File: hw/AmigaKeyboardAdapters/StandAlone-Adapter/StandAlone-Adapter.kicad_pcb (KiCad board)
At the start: 2 copper layers, 78.7 x 58.4 mm, 56 parts, among them J1 RJ12, J2 Conn_02x03_Odd_Even, P1 CONN_01X02, Q1 BSS138, Q2 BSS138, Q3 BSS138, U1 AZ1117-3.3, U3 STM32F401RCTx

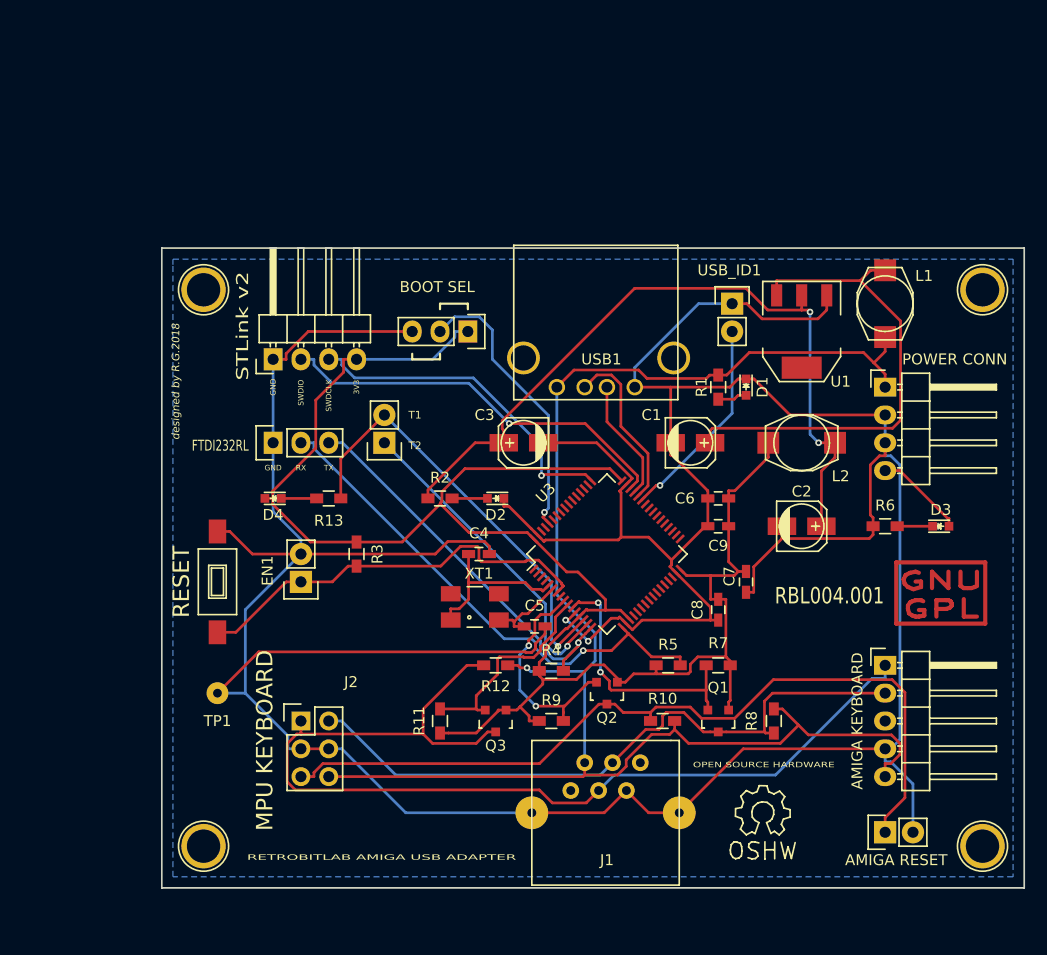
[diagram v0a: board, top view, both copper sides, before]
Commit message: Modified for USB Host A and RJ10 Connectors
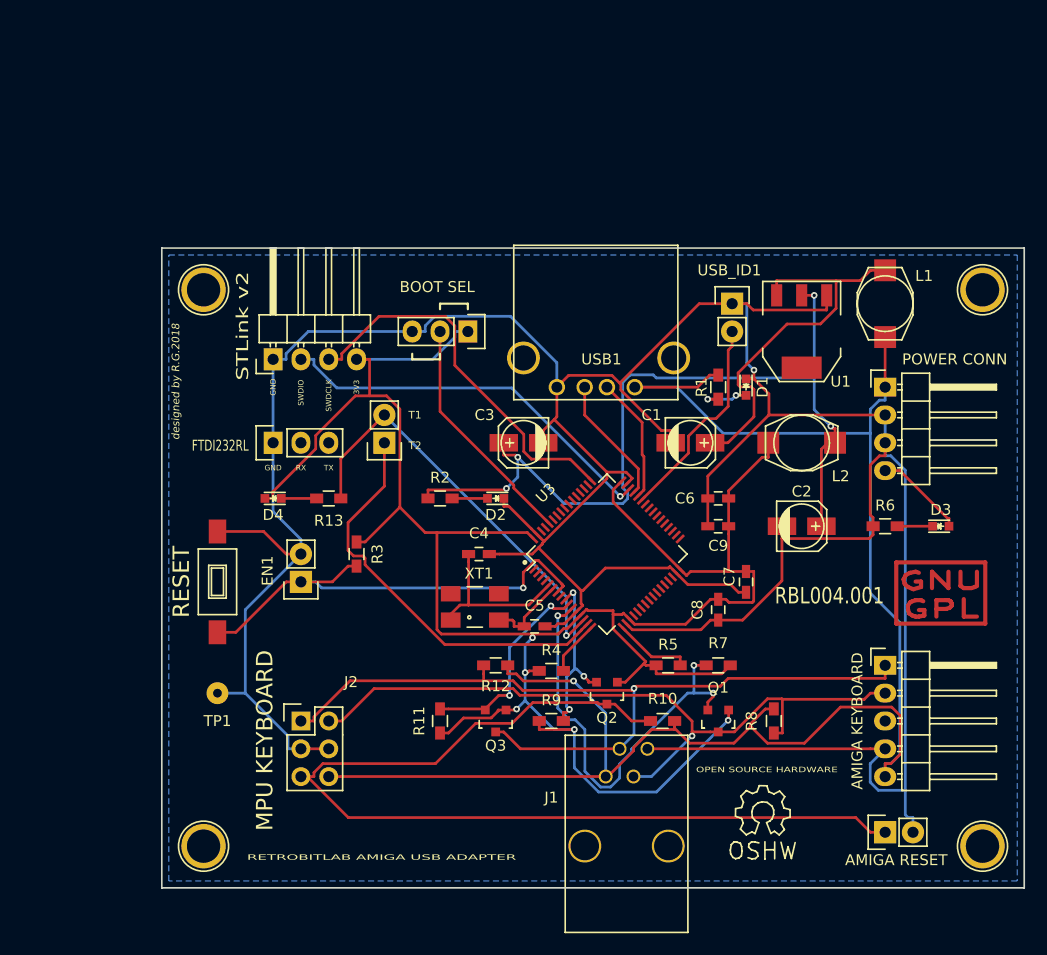
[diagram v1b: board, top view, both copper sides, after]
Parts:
- J1: value RJ12 -> RJ10; footprint Connect:RJ12_E -> RetroBitLab:RJ10-RECEPTACLE-Assmann-ASS-2004-3-4-LP-N-R
- moved J1 12.0 mm to (158.8, 130.8)
- renumbered G*** to AMIGALOGO, REF** to GNUGPL, G*** to WORKBENCHLOGO
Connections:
- DEBUG1 pad 2: UART_RX_TTL -> (no net)
- DEBUG1 pad 3: UART_TX_TTL -> (no net)
- J1 pad 1: (no net) -> VCC5V
- J1 pad 2: VCC5V -> KBD_CLOCK
- J1 pad 3: KBD_CLOCK -> KBD_DATA
- J1 pad 4: KBD_DATA -> GND
- J1 pad 5: GND -> (no net)
- R4 pad 2: UART_TX_TTL -> /USART3_TX
- R5 pad 2: UART_RX_TTL -> /USART3_RX
- U3 pad 16: UART_TX_TTL -> /USART3_TX
- U3 pad 17: UART_RX_TTL -> /USART3_RX
- USB1 pad 1: GND -> VCC5V
- USB1 pad 2: USB_P -> USB_N
- USB1 pad 3: USB_N -> USB_P
- USB1 pad 4: VCC5V -> GND
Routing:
- net UART_RX_TTL: track 47.2 -> 0.00 mm, vias 1 -> 0
- net GND: track 371.1 -> 332.7 mm, vias 2 -> 1
- net UART_TX_TTL: track 37.1 -> 0.00 mm, vias 1 -> 0
- net VCC3V3: track 167.8 -> 203.1 mm, vias 0 -> 5
- net KBD_CLOCK: track 95.6 -> 76.5 mm, vias 0 -> 1
- net KBD_3v3_DATA: track 23.9 -> 39.4 mm, vias 2 -> 3
- net KBD_RESET: track 75.3 -> 90.5 mm
- net VCC5V: track 144.9 -> 159.1 mm
- net Net-(C2-Pad1): track 68.8 -> 78.7 mm, vias 2 -> 4
- net +5V: track 44.8 -> 35.7 mm
- net TP2: track 30.1 -> 37.8 mm, vias 1 -> 0
- net /USART3_RX: track 0.00 -> 7.20 mm
- net KBD_DATA: track 60.5 -> 66.8 mm, vias 0 -> 1
- net Net-(EN1-Pad1): track 37.9 -> 43.1 mm, vias 0 -> 1
- net /USART3_TX: track 0.00 -> 5.06 mm
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
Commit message: The Debug UART Pins (RX & TX) were left unconnected
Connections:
- DEBUG1 pad 2: (no net) -> UART_RX_TTL
- DEBUG1 pad 3: (no net) -> UART_TX_TTL
- R4 pad 2: /USART3_TX -> UART_TX_TTL
- R5 pad 2: /USART3_RX -> UART_RX_TTL
- U3 pad 16: /USART3_TX -> UART_TX_TTL
- U3 pad 17: /USART3_RX -> UART_RX_TTL
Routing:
- net UART_RX_TTL: track 0.00 -> 150.0 mm, vias 0 -> 4
- net UART_TX_TTL: track 0.00 -> 78.3 mm, vias 0 -> 1
- net /USART3_RX: track 7.20 -> 0.00 mm
- net /USART3_TX: track 5.06 -> 0.00 mm
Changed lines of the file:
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@@
 (kicad_pcb (version 4) (host pcbnew 4.0.2+dfsg1-stable)
   (general
-    (links 108)
+    (links 110)
     (no_connects 0)
     (area 121.844999 86.284999 200.735001 144.855001)
     (thickness 1.6)
     (drawings 35)
-    (tracks 550)
+    (tracks 583)
     (zones 0)
     (modules 56)
@@
     (34 B.Paste user)
     (35 F.Paste user)
-    (36 B.SilkS user)
-    (37 F.SilkS user)
+    (36 B.SilkS user hide)
+    (37 F.SilkS user hide)
     (38 B.Mask user)
     (39 F.Mask user)
@@
   (net 26 USB_N)
   (net 27 USB_P)
-  (net 28 /USART3_TX)
-  (net 29 /USART3_RX)
+  (net 28 UART_RX_TTL)
+  (net 29 UART_TX_TTL)
   (net_class Default "This is the default net class."
     (clearance 0.2)
@@
     (uvia_drill 0.1)
     (add_net +5V)
-    (add_net /USART3_RX)
-    (add_net /USART3_TX)
     (add_net BOOT0)
     (add_net GND)
@@
     (add_net TP1)
     (add_net TP2)
+    (add_net UART_RX_TTL)
+    (add_net UART_TX_TTL)
     (add_net USB_ID)
     (add_net USB_N)
@@
     (pad 1 thru_hole rect (at 0 0 90) (size 2.032 1.7272) (drill 1.016) (layers *.Cu *.Mask F.SilkS)
       (net 3 GND))
-    (pad 2 thru_hole oval (at 0 2.54 90) (size 2.032 1.7272) (drill 1.016) (layers *.Cu *.Mask F.SilkS))
-    (pad 3 thru_hole oval (at 0 5.08 90) (size 2.032 1.7272) (drill 1.016) (layers *.Cu *.Mask F.SilkS))
+    (pad 2 thru_hole oval (at 0 2.54 90) (size 2.032 1.7272) (drill 1.016) (layers *.Cu *.Mask F.SilkS)
+      (net 28 UART_RX_TTL))
+    (pad 3 thru_hole oval (at 0 5.08 90) (size 2.032 1.7272) (drill 1.016) (layers *.Cu *.Mask F.SilkS)
+      (net 29 UART_TX_TTL))
     (model Pin_Headers.3dshapes/Pin_Header_Straight_1x03.wrl
       (at (xyz 0 -0.1 0))
@@
       (net 5 VCC3V3))
     (pad 2 smd rect (at 1.1 0) (size 1.2 0.9) (layers F.Cu F.Paste F.Mask)
-      (net 28 /USART3_TX))
+      (net 29 UART_TX_TTL))
     (model Resistors_SMD.3dshapes/R_0603_HandSoldering.wrl
       (at (xyz 0 0 0))
@@
       (net 5 VCC3V3))
     (pad 2 smd rect (at 1.1 0) (size 1.2 0.9) (layers F.Cu F.Paste F.Mask)
-      (net 29 /USART3_RX))
+      (net 28 UART_RX_TTL))
     (model Resistors_SMD.3dshapes/R_0603_HandSoldering.wrl
       (at (xyz 0 0 0))
@@
       (net 24 TP2))
     (pad 16 smd rect (at -5.7 3.75 45) (size 1 0.25) (layers F.Cu F.Paste F.Mask)
-      (net 28 /USART3_TX))
+      (net 29 UART_TX_TTL))
     (pad 17 smd rect (at -3.75 5.7 135) (size 1 0.25) (layers F.Cu F.Paste F.Mask)
-      (net 29 /USART3_RX))
+      (net 28 UART_RX_TTL))
     (pad 18 smd rect (at -3.25 5.7 135) (size 1 0.25) (layers F.Cu F.Paste F.Mask)
       (net 3 GND))
@@
   (segment (start 160.5271 101.6083) (end 165.4254 106.5066) (width 0.25) (layer F.Cu) (net 27))
   (segment (start 160.5271 99.0621) (end 160.5271 101.6083) (width 0.25) (layer F.Cu) (net 27))
-  (segment (start 158.58 123.5833) (end 158.58 124.968) (width 0.25) (layer F.Cu) (net 28))
-  (segment (start 161.1811 120.9822) (end 158.58 123.5833) (width 0.25) (layer F.Cu) (net 28))
-  (segment (start 166.6414 123.6847) (end 169.248 123.6847) (width 0.25) (layer F.Cu) (net 29))
-  (segment (start 163.9389 120.9822) (end 166.6414 123.6847) (width 0.25) (layer F.Cu) (net 29))
-  (segment (start 169.248 124.46) (end 169.248 123.6847) (width 0.25) (layer F.Cu) (net 29))
+  (segment (start 169.248 124.46) (end 169.248 122.8295) (width 0.25) (layer F.Cu) (net 28) (status 400000))
+  (segment (start 134.62 101.6) (end 134.62 104.14) (width 0.25) (layer F.Cu) (net 28) (status 800000))
+  (segment (start 134.5565 101.5365) (end 134.62 101.6) (width 0.25) (layer F.Cu) (net 28))
+  (segment (start 129.032 101.5365) (end 134.5565 101.5365) (width 0.25) (layer F.Cu) (net 28))
+  (via (at 129.032 101.5365) (size 0.6) (drill 0.4) (layers F.Cu B.Cu) (net 28))
+  (segment (start 129.032 89.2175) (end 129.032 101.5365) (width 0.25) (layer B.Cu) (net 28))
+  (segment (start 129.6035 88.646) (end 129.032 89.2175) (width 0.25) (layer B.Cu) (net 28))
+  (segment (start 183.3245 88.646) (end 129.6035 88.646) (width 0.25) (layer B.Cu) (net 28))
+  (segment (start 185.4835 90.805) (end 183.3245 88.646) (width 0.25) (layer B.Cu) (net 28))
+  (via (at 185.4835 90.805) (size 0.6) (drill 0.4) (layers F.Cu B.Cu) (net 28))
+  (segment (start 192.0875 90.805) (end 185.4835 90.805) (width 0.25) (layer F.Cu) (net 28))
+  (segment (start 197.104 95.8215) (end 192.0875 90.805) (width 0.25) (layer F.Cu) (net 28))
+  (segment (start 197.104 112.649) (end 197.104 95.8215) (width 0.25) (layer F.Cu) (net 28))
+  (segment (start 196.215 113.538) (end 197.104 112.649) (width 0.25) (layer F.Cu) (net 28))
+  (segment (start 185.4835 113.538) (end 196.215 113.538) (width 0.25) (layer F.Cu) (net 28))
+  (segment (start 185.1025 113.919) (end 185.4835 113.538) (width 0.25) (layer F.Cu) (net 28))
+  (via (at 185.1025 113.919) (size 0.6) (drill 0.4) (layers F.Cu B.Cu) (net 28))
+  (segment (start 185.1025 114.681) (end 185.1025 113.919) (width 0.25) (layer B.Cu) (net 28))
+  (segment (start 177.6095 122.174) (end 185.1025 114.681) (width 0.25) (layer B.Cu) (net 28))
+  (segment (start 169.8625 122.174) (end 177.6095 122.174) (width 0.25) (layer B.Cu) (net 28))
+  (segment (start 169.2275 122.809) (end 169.8625 122.174) (width 0.25) (layer B.Cu) (net 28))
+  (via (at 169.2275 122.809) (size 0.6) (drill 0.4) (layers F.Cu B.Cu) (net 28))
+  (segment (start 169.248 122.8295) (end 169.2275 122.809) (width 0.25) (layer F.Cu) (net 28))
+  (segment (start 166.6414 123.6847) (end 169.248 123.6847) (width 0.25) (layer F.Cu) (net 28))
+  (segment (start 163.9389 120.9822) (end 166.6414 123.6847) (width 0.25) (layer F.Cu) (net 28))
+  (segment (start 169.248 124.46) (end 169.248 123.6847) (width 0.25) (layer F.Cu) (net 28))
+  (segment (start 158.58 124.968) (end 158.58 124.29) (width 0.25) (layer F.Cu) (net 29) (status 400000))
+  (segment (start 137.16 100.711) (end 137.16 104.14) (width 0.25) (layer B.Cu) (net 29) (status 800000))
+  (segment (start 137.033 100.584) (end 137.16 100.711) (width 0.25) (layer B.Cu) (net 29))
+  (via (at 137.033 100.584) (size 0.6) (drill 0.4) (layers F.Cu B.Cu) (net 29))
+  (segment (start 126.365 100.584) (end 137.033 100.584) (width 0.25) (layer F.Cu) (net 29))
+  (segment (start 124.1425 102.8065) (end 126.365 100.584) (width 0.25) (layer F.Cu) (net 29))
+  (segment (start 124.1425 122.936) (end 124.1425 102.8065) (width 0.25) (layer F.Cu) (net 29))
+  (segment (start 124.3965 123.19) (end 124.1425 122.936) (width 0.25) (layer F.Cu) (net 29))
+  (segment (start 157.48 123.19) (end 124.3965 123.19) (width 0.25) (layer F.Cu) (net 29))
+  (segment (start 158.58 124.29) (end 157.48 123.19) (width 0.25) (layer F.Cu) (net 29))
+  (segment (start 158.58 123.5833) (end 158.58 124.968) (width 0.25) (layer F.Cu) (net 29))
+  (segment (start 161.1811 120.9822) (end 158.58 123.5833) (width 0.25) (layer F.Cu) (net 29))
   (zone (net 3) (net_name GND) (layer B.Cu) (hatch edge 0.508)
     (connect_pads (clearance 0.508))

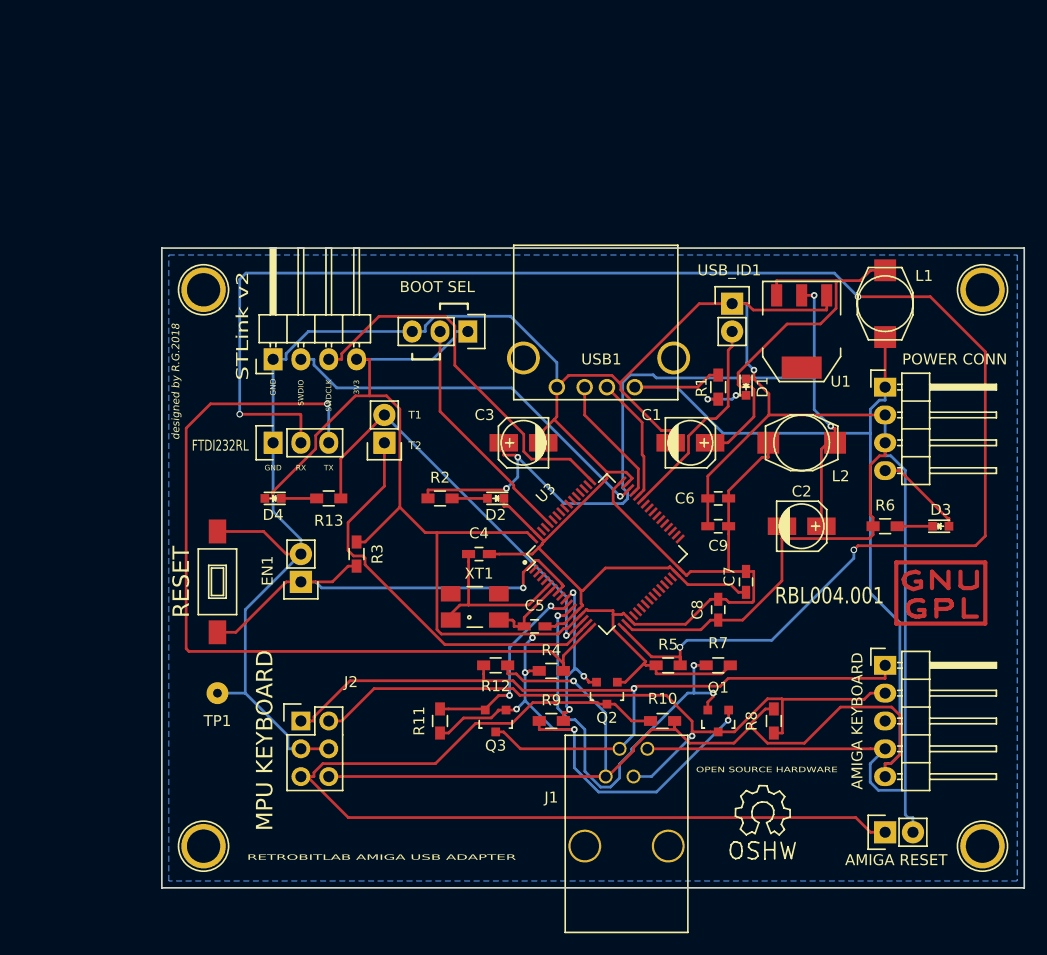
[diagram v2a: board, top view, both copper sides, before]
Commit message: Added all kicad libraries
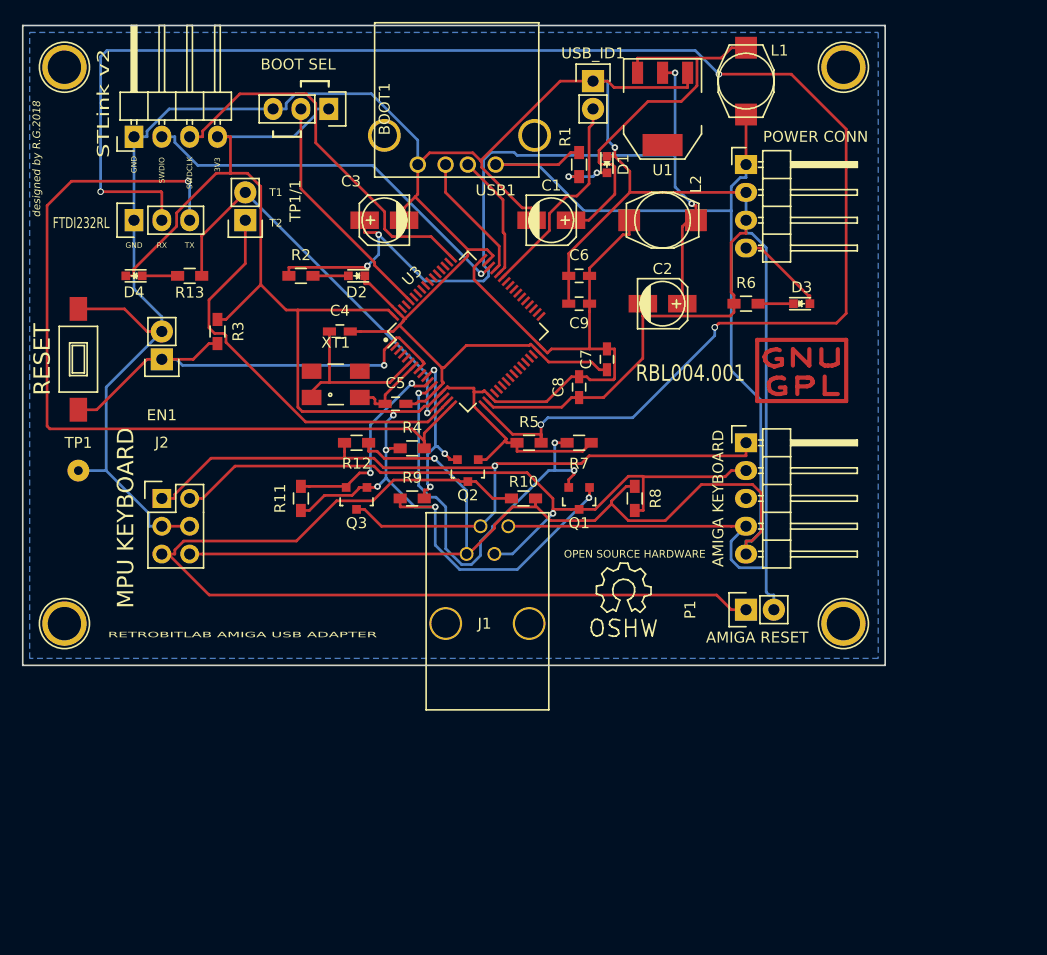
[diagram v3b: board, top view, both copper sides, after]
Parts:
- moved AMIGALOGO 24.0 mm to (151.1, 86.4)
- moved BOOT1 24.0 mm to (137.2, 73.7)
- moved C1 24.0 mm to (157.5, 83.8)
- moved C2 24.0 mm to (167.6, 91.4)
- moved DEBUG1 24.0 mm to (119.4, 83.8)
- moved L2 24.0 mm to (167.6, 83.8)
- moved POWER1 24.0 mm to (175.3, 78.7)
- moved R6 24.0 mm to (175.3, 91.4)
- moved TP1/1 24.0 mm to (129.5, 83.8)
- moved U1 24.0 mm to (167.6, 73.7)
- moved XT1 24.0 mm to (137.8, 98.8)
- moved EN1 24.0 mm to (121.9, 96.5)
- moved H1 24.0 mm to (113.0, 69.8)
- moved RESET1 24.0 mm to (114.3, 96.5)
- moved AMIGA_KEYBOARD1 24.0 mm to (175.3, 104.1)
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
